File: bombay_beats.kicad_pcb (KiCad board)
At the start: 2 copper layers, 154.9 x 17.8 mm, 23 parts, among them SW1 SW_Push_Dual, SW2 SW_Push_Dual, SW3 SW_Push_Dual, SW4 SW_Push_Dual, SW5 SW_Push_Dual, SW6 SW_Push_Dual, SW7 SW_Push_Dual, SW8 SW_Push_Dual, SW9 SW_SPDT, U1 74HC165

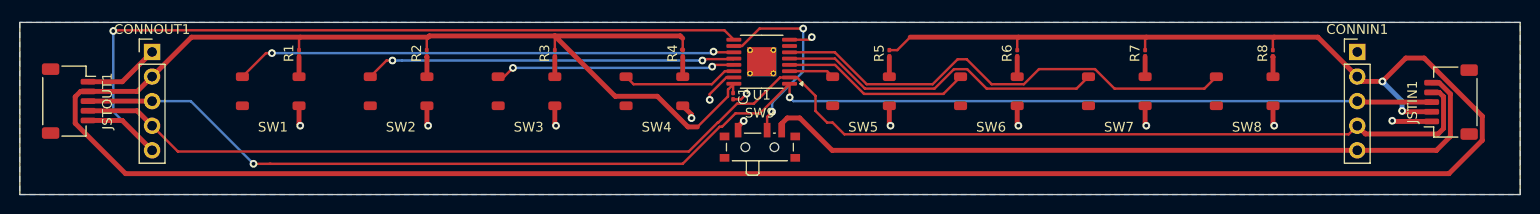
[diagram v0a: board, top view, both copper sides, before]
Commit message: fix 0603 footprints
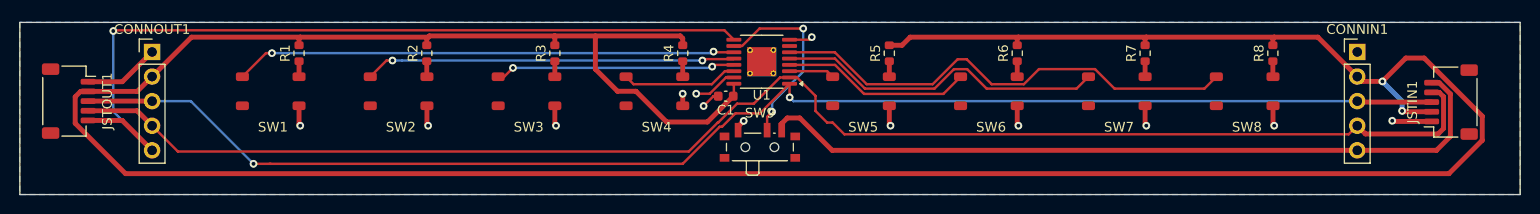
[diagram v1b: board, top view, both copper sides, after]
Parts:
- C1: footprint Capacitor_SMD:C_0201_0603Metric -> Capacitor_SMD:C_0603_1608Metric
- R1, R2, R3, R4, R5, R6, R7, R8: footprint Resistor_SMD:R_0201_0603Metric -> Resistor_SMD:R_0603_1608Metric
- moved C1 0.76 mm to (128.8, 81.3), turned to 180 degrees
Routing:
- net VCC: track 328.8 -> 322.1 mm
- net GND: track 37.4 -> 38.1 mm

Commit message: fix pinout of jst input
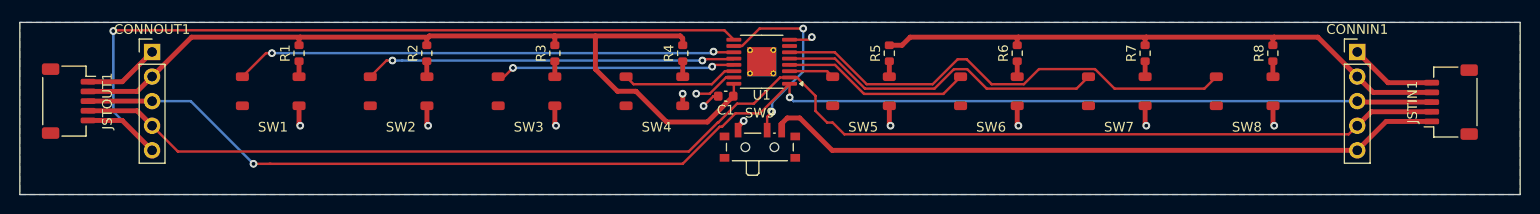
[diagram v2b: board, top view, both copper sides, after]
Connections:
- JSTIN1 pad 1: GND -> /DATA_IN
- JSTIN1 pad 2: VCC -> /DATA_CLK
- JSTIN1 pad 4: /DATA_CLK -> VCC
- JSTIN1 pad 5: /DATA_IN -> GND
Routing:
- net VCC: track 322.1 -> 151.2 mm, vias 2 -> 0
- net /DATA_IN: track 78.8 -> 70.7 mm
- net /DATA_CLK: track 153.9 -> 148.0 mm
- net GND: track 38.1 -> 43.0 mm, vias 13 -> 12
